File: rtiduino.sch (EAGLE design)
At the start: 111 parts, among them IC7 LM358D, J1 DCJ0202, J2 3.5MM-JACK, J3 2.5MM-JACK, Q2 16MHz, T1 NDT2955, T2 FDN340P, U1 ATMEGA2560AU, U10 AQV252G, U11 AQV252G, U12 AQV252G, U13 AQV252G, U14 AQV252G, U15 AQV252G, U16 AQV252G, U17 AQV252G, U2 LDU240S500, U20 AQV252G, U21 AQV252G, U22 AQV252G, U23 AQV252G, U24 AQV252G, U25 AQV252G, U26 AQV252G, U27 AQV252G, U3 LM2594HVM-3.3, U30 AQV252G, U31 AQV252G, U32 AQV252G, U33 AQV252G, U34 AQV252G, U35 AQV252G, U36 AQV252G, U37 AQV252G, U4 FT232RL, U5 FOD852

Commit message: Latest version with * fixed PSU arrangement * more caps * connectors moved outwards
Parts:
- removed C18: (no value), resistor:C-EUC0805K
- removed IC7: LM358D, linear:LM358D
- removed R10, R6: 10k, rcl:R-EU_R0805
- removed RESET-EN: (no value), jumper:SJ
- removed SV1: (no value), con-lstb:MA03-1
- removed T1: NDT2955, zetex:PMOSSOT223
- removed T2: FDN340P, zetex:PMOSSOT23
- removed U2: LDU240S500, RTI:LDU240S500
- added C19, C20, C21: (no value), resistor:C-EUC1210K
- added C22: (no value), rcl:C-EUC0805K
- added C23: 68uF, rcl:CPOL-EUE5-13
- added D3: SF37, farnell-parts:SF37
- added JP1: (no value), jumper:JP2E
- added L2: (no value), rcl:L-EU6000-XXX-RC
- added PAD1: VIN, wirepad:WIREPAD4,16O1,6
- added PAD2: GND, wirepad:WIREPAD4,16O1,6
- added PAD3: LED_VCC, wirepad:WIREPAD4,16O1,6
- added PAD4: LED_GND, wirepad:WIREPAD4,16O1,6
- added R2: 0R, resistor:R-EU_R0805
- C1, C10, C11, C14, C15, C16, C2, C3, C4, C9: device rcl:C-EU -> rcl:C-EUC0805K
- C12, C17: value 100n -> (none); device rcl:C-EU -> resistor:C-EUC1210K
- C13: value 100n -> (none); device rcl:C-EU -> rcl:C-EUC0805K
- C5: device resistor:CPOL-EUE3.5-10 -> rcl:CPOL-EUE5-13
- C8: device resistor:C-EUC0805K -> resistor:C-EUC1210K
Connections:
- removed net 5VREG: C18.1, C6.+, C7.+, C8.1, L1.2, R10.2, TP1.TP, U3.FB
- removed net CMP: C13.2, IC7A.+IN, R10.1, R6.2
- removed net DTR: C12.1, RESET-EN.1, RESET-EN.2, U4.DTR#
- removed net GATE_CMD: IC7B.-IN, IC7B.OUT, T1.G, T2.G
- removed net RXD3: R11.2, U1.PJ0(RXD3/PCINT9)
- removed net TXD3: R12.2, U1.PJ1(TXD3/PCINT10)
- new net RXD: JP1.1, R11.2, U1.(RXD1/INT2)PD2, U1.PJ0(RXD3/PCINT9)
- new net TXD: JP1.2, R12.2, U1.(TXD1/INT3)PD3, U1.PJ1(TXD3/PCINT10)
- net +3V3: no longer IC7A.-IN
- net +5V: now also C12.1, C6.+, C7.+, C8.1, L1.2, R2.1, R2.2, TP1.TP, U3.FB; no longer C16.1, C17.2, IC7P.V+, R7.2, R9.2, T1.S, T2.S, U4.RESET#, U4.VCC5I, U4.VCCIO
- net GND: now also C12.2, C13.2, C17.2, C19.2, C20.2, C21.2, C22.2, C23.-, JP1.3, PAD2.P; no longer C13.1, C17.1, C18.2, IC7P.V-, R6.1, SV1.1, U2.-VIN, U2.-VIN_2
- net LED_GND: now also PAD4.P; no longer U2.-VOUT, U2.-VOUT_2
- net LED_VCC: now also PAD3.P; no longer U2.+VOUT, U2.+VOUT_2
- net N$4: now also C20.1, C21.1, C22.1, C23.+, D3.C, L2.1; no longer IC7A.OUT, IC7B.+IN
- net N$43: now also C13.1, C17.1, C19.1, L2.2, U3.VIN; no longer S1.P, S1.P1
- net RESET: now also S1.P, S1.P1; no longer C12.2
- net RXD2: no longer SV1.3
- net TXD2: no longer SV1.2
- net USBVCC: now also C16.1, R7.2, R9.2, U4.RESET#, U4.VCC5I, U4.VCCIO; no longer T1.D, T2.D
- net VIN: now also D3.A, PAD1.P; no longer U2.+VIN, U2.+VIN_2, U3.VIN
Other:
- moved on the sheet: C5

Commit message: Update wih Superdome PCB
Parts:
- removed C13, C22: (no value), rcl:C-EUC0805K
- removed C17, C19, C20, C21: (no value), resistor:C-EUC1210K
- removed C23: 68uF, rcl:CPOL-EUE5-13
- removed D1: 1N5817-B, diode:1N5817-B
- removed D3: SF37, farnell-parts:SF37
- removed PAD1: VIN, wirepad:WIREPAD4,16O1,6
- removed PAD2: GND, wirepad:WIREPAD4,16O1,6
- removed PAD3: LED_VCC, wirepad:WIREPAD4,16O1,6
- removed PAD4: LED_GND, wirepad:WIREPAD4,16O1,6
- removed R2: 0R, resistor:R-EU_R0805
- added C18, C24, C25, C26, C27, C28, C30, C31: 100nF, rcl:C-EUC0805K
- added C29, C32: 4.7uF, rcl:C-EUC0805K
- added C42, C43, C44, C45, C46: 100n, rcl:C-EUC0805K
- added D4: BAT54C, diode:BAT54C
- added D5: MBRS130, diode:DIODE-DO214AA
- added F2: 500mA, rcl:L-EUL1812
- added J4: USB PROG, CC11x:47346-0001
- added JP2: (no value), pinhead:PINHD-1X6
- added JP3: (no value), pinhead:PINHD-2X8
- added L3: 330uH (DO3308P-334), inductor-coilcraft:DO3316P
- added R10: 10K, resistor:R-EU_R0805
- added R3, R6: 1k, rcl:R-EU_R0805
- added R40, R41: 1K, resistor:R-EU_R0805
- added R42, R43, R44, R45, R46: 10k, resistor:R-EU_R0805
- added R8: 4K7, resistor:R-EU_R0805
- added RESET-EN: (no value), jumper:SJ
- added RX1, TX1: (no value), led:LED0805ROUND
- added U2: FT232RL, SmartPrj:FT232RL
- added U6: LED-DRIVER, RTI:LED-DRIVER
- C12: value (none) -> 10UF; device resistor:C-EUC1210K -> RTI:EEE-FK1J100P-CASE-D
- C6: device resistor:CPOL-EUR/2012-12R -> rcl:CPOL-EUE5-13
- C7: value 68uF -> 100uF; device resistor:CPOL-EUR/2012-12R -> rcl:CPOL-EUE5-13
- C8: value (none) -> 47UF; device resistor:C-EUC1210K -> RTI:EEE-FK1J470P-CASE-F
- J3: value 2.5MM-JACK -> 2.5MM-JACKPRO; device RTI:2.5MM-JACK -> RTI:2.5MM-JACKPRO
- L1: value 100uH -> 3uH; device inductors:SBC10 -> RTI:WE-TPC-744053003_5818/5828
- L2: value (none) -> DR73-680-R; device rcl:L-EU6000-XXX-RC -> RTI:DR73-680-R
- U3: value LM2594HVM-3.3 -> LM2594HVM-5.0
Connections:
- new net +3V3PROG: C24.2, U2.VCC30
- new net N$50: RX1.C, U2.GPIO1
- new net N$52: TX1.C, U2.GPIO0
- new net N$58: R3.1, RX1.A
- new net N$62: R6.1, TX1.A
- new net N$63: F2.2, J4.1
- new net N$66: C26.1, RESET-EN.1, RESET-EN.2, U2.DTR#
- new net N$68: C16.2, R10.1, R8.2, U4.RESET#
- new net PROG_D+: J4.3, U2.USBDP
- new net PROG_D-: J4.2, U2.USBDM
- new net RXD1: U1.(RXD1/INT2)PD2
- new net RXDP: JP2.4, R40.1, U2.TXD
- new net RXD_PROG: R40.2, U1.(RXD0/PCIN8)PE0
- new net SCL: JP3.1, U1.(SCL/INT0)PD0
- new net SDA: JP3.3, U1.(SDA/INT1)PD1
- new net SW1: C46.1, JP3.7, R46.2, U1.PK0(ADC8/PCINT16)
- new net SW2: C45.1, JP3.9, R45.2, U1.PK1(ADC9/PCINT17)
- new net SW3: C44.1, JP3.11, R44.2, U1.PK2(ADC10/PCINT18)
- new net SW4: C43.1, JP3.13, R43.2, U1.PK3(ADC11/PCINT19)
- new net SW5: C42.1, JP3.15, R42.2, U1.PK4(ADC12/PCINT20)
- new net TXD1: U1.(TXD1/INT3)PD3
- new net TXDP: JP2.5, R41.1, U2.RXD
- new net TXD_PROG: R41.2, U1.(TXD0)PE1
- new net USBPROGVCC: C18.1, C25.1, C30.1, C31.1, C32.1, D4.A2, F2.1, JP2.3, R3.2, R6.2, U2.RESET#, U2.VCC5I, U2.VCCIO
- net +5V: now also C27.1, C28.1, C29.1, D4.CC, JP3.2, R42.1, R43.1, R44.1, R45.1, R46.1, U4.VCC5I, U4.VCCIO; no longer C12.1, C6.+, C8.1, R2.1, R2.2, U3.FB
- net GND: now also C16.1, C18.2, C24.1, C25.2, C27.2, C28.2, C29.2, C30.2, C31.2, C32.2, C42.2, C43.2, C44.2, C45.2, C46.2, D5.A, J4.5, JP2.1, JP3.10, JP3.12, JP3.14, JP3.16, JP3.4, JP3.8, R10.2, U2.AGND, U2.GND1, U2.GND2, U2.GND3, U2.TEST, U6.GIN; no longer C13.2, C16.2, C17.2, C19.2, C20.2, C21.2, C22.2, C23.-, D1.A, PAD2.P
- net LED_GND: now also U6.GOUT; no longer PAD4.P
- net LED_VCC: now also U6.VOUT; no longer PAD3.P
- net N$4: now also C6.+, L1.1, L3.2, U3.FB; no longer C20.1, C21.1, C22.1, C23.+, D3.C, L2.1
- net N$43: now also C8.1, L2.1, U6.VIN; no longer C13.1, C17.1, C19.1, L2.2, U3.VIN
- net N$48: now also D5.C, L3.1; no longer D1.C, L1.1
- net RESET: now also C26.2
- net RXD: no longer U1.(RXD1/INT2)PD2
- net RXD2: now also JP3.6
- net TXD: no longer U1.(TXD1/INT3)PD3
- net TXD2: now also JP3.5
- net USBVCC: now also D4.A1, R8.1; no longer C16.1, U4.RESET#, U4.VCC5I, U4.VCCIO
- net VIN: now also C12.1, L2.2, U3.VIN; no longer D3.A, PAD1.P
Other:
- note added: "** This is a 5V reg !! ** Keep leads as short as possible. Use isolated ground plane."
- note added: "30V Input"
- note added: "5V uC Switchmode Powersupply"
- note added: "Camera Shutter"
- note added: "Control Interface"
- note added: "Display Serial"
- note added: "Fire Button"
- note added: "Header for FTDI TTL-232R-5V cable. Needs manual reset as DTR is not connected."
- note added: "ICSP"
- note added: "LED Constant Current Driver"
- note added: "Onecall: 1267387"
- note added: "Onecall: 2082565"
- note added: "Onecall: 2457508"
- note added: "Onecall: 8812667"
- note added: "Onecall: 8812675"
- note added: "Pinout for FEMALE D-Sub connectors on PCB"
- note added: "Place close to U2"
- note added: "Place close to U4"
- note added: "Programming/Debug Interfaces"
- note added: "RS: 715-3031"
- note added: "Screen Interface"
- note added: "Status LEDs"
- note added: "UI Switches"
- note added: "USB Arduino Programmer"
- note added: "USB Voltage Combiner"
- note removed: "LED PSU"
- note removed: "This is the pin out if FEMALE D-subs are used on the PCB"
- note removed: "This is the pin out if FEMALE d-subs are used on the board"

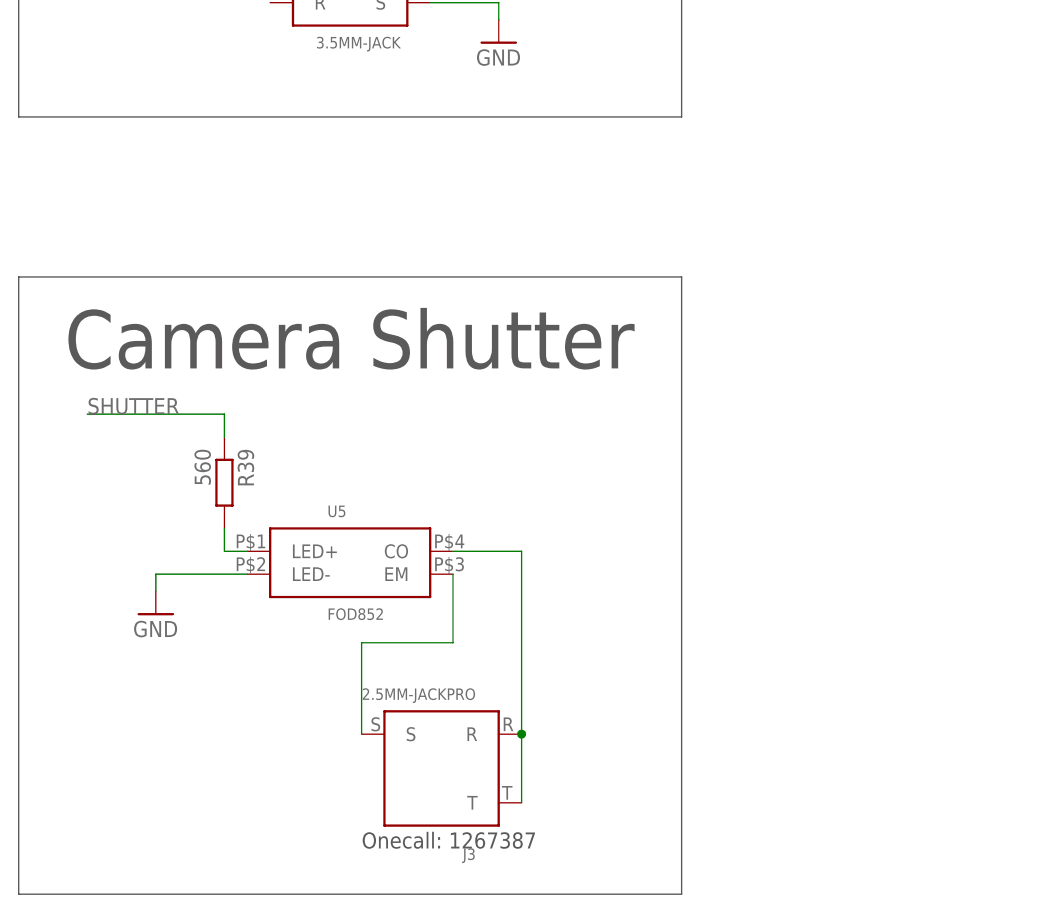
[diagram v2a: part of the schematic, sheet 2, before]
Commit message: Tweak to camera shutter trigger (split focus and shutter), tweak to serial programming, misc fixes
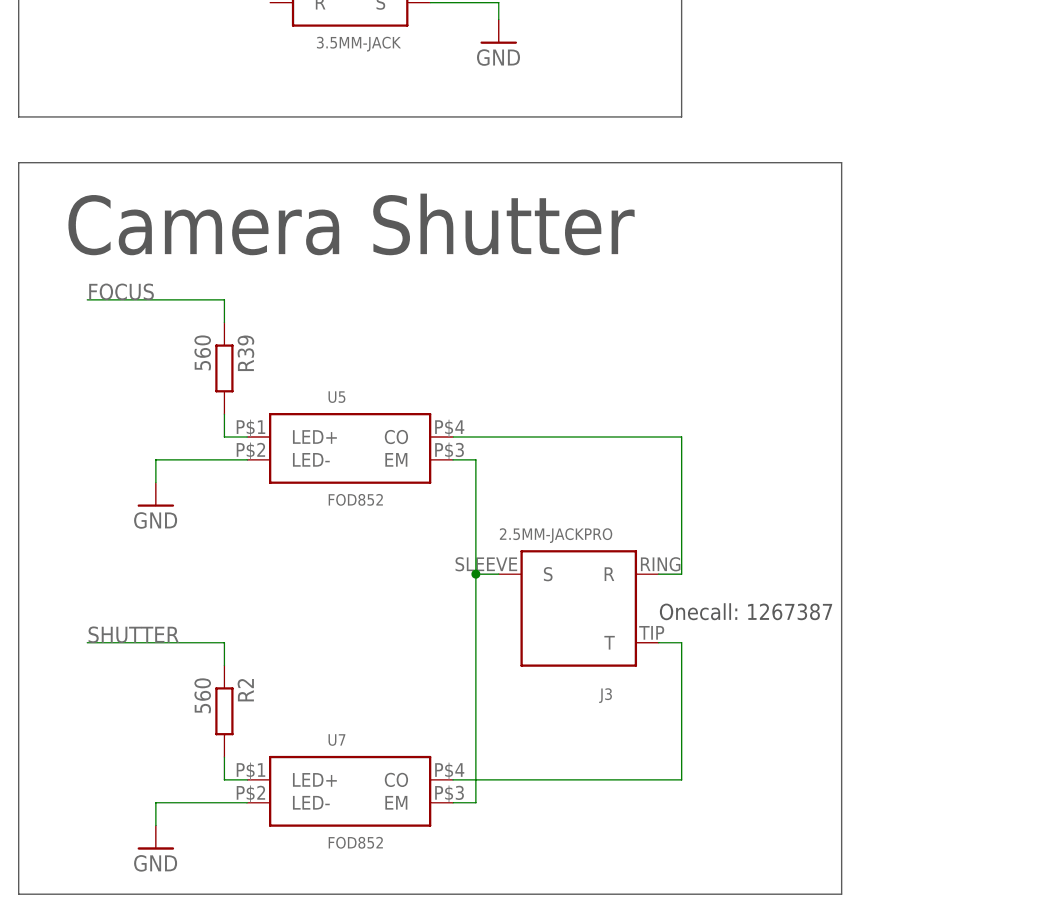
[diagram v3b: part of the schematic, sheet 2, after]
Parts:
- added C13: 100nF, rcl:C-EUC0805K
- added R2: 560, resistor:R-EU_R0805
- added RESET-EN1: (no value), jumper:SJ
- added U7: FOD852, RTI:FOD852
- L, RX, RX1, TX, TX1: device led:LED0805ROUND -> led:LEDCHIP-LED0805
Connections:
- net N$66 renamed DTR
- removed net N$51: J3.R, J3.T, U5.CO
- new net CAM_GND: J3.S, U5.EM, U7.EM
- new net CAM_RING: J3.R, U5.CO
- new net CAM_SHUTTER: J3.T, U7.CO
- new net DTRP: C13.1, JP2.2, RESET-EN1.1, RESET-EN1.2
- new net FOCUS: R39.1, U1.(TOSC2)PG3
- net GND: now also U7.LED-
- net N$61: now also R2.2, U7.LED+; no longer J3.S, U5.EM
- net RESET: now also C13.2
- net SHUTTER: now also R2.1; no longer R39.1
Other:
- moved on the sheet: J3, R39, U5

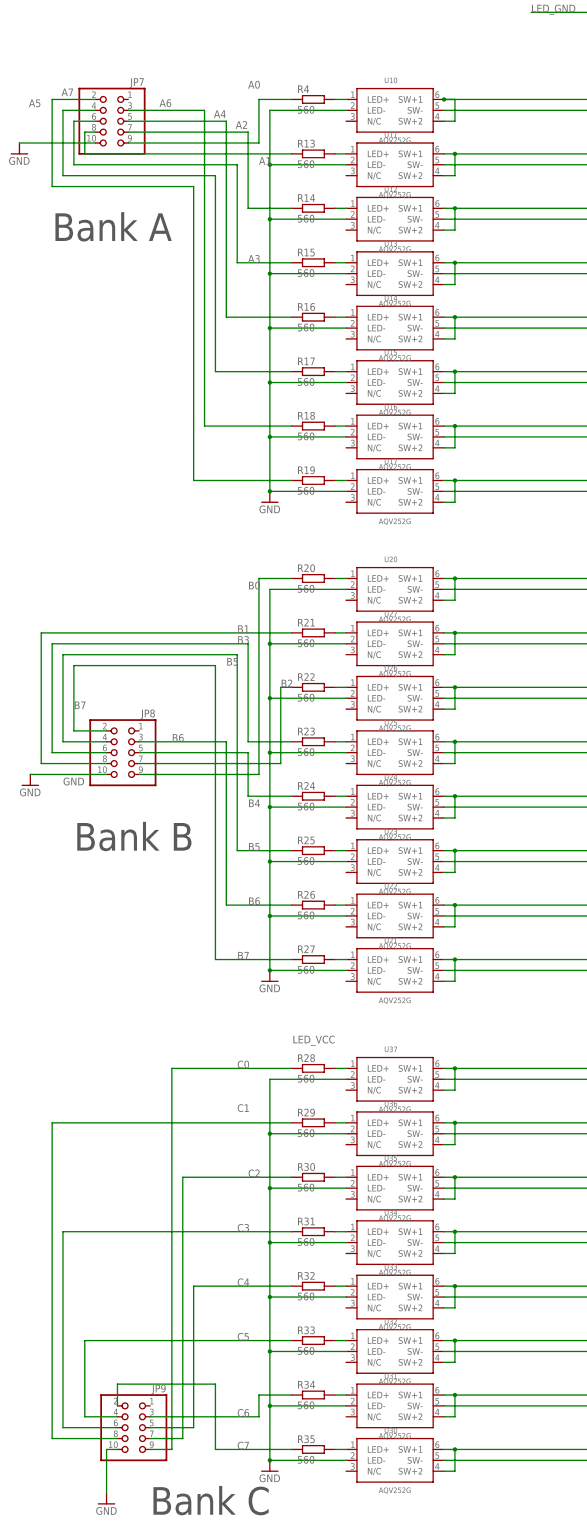
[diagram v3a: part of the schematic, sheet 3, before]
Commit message: Version 1.3 of RTIDuino and updated order sheet
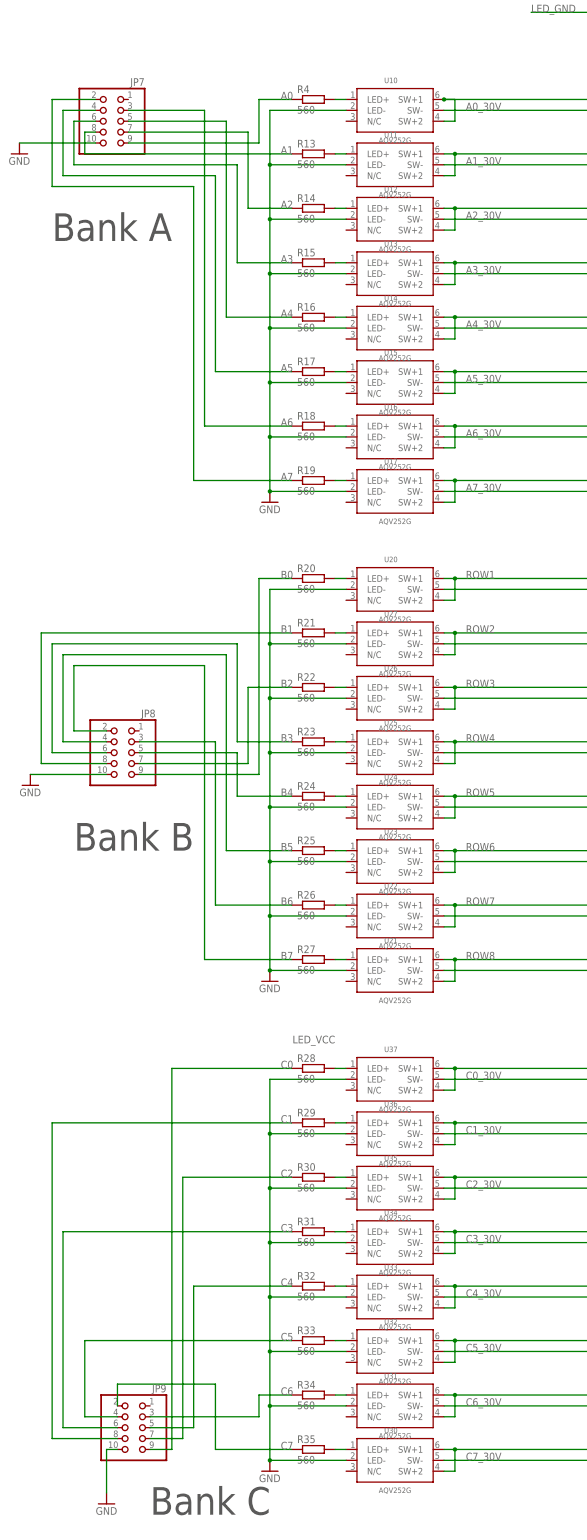
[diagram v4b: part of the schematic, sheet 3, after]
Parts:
- added JP4: (no value), pinhead:PINHD-1X2
- C1, C10, C14, C15, C16, C4, C42, C43, C44, C45, C46, C9: value 100n -> 100nF
- C11, C2, C3: value 22p -> 22pF
- C12: value 10UF -> 10uF
- C8: value 47UF -> 47uF
- R3, R6, R7, R9: value 1k -> 1K
- R42, R43, R44, R45, R46: value 10k -> 10K
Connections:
- net N$11 renamed A4_30V
- net N$14 renamed C6_30V
- net N$33 renamed A0_30V
- net N$34 renamed C0_30V
- net N$35 renamed A1_30V
- net N$36 renamed A2_30V
- net N$37 renamed A3_30V
- net N$38 renamed C2_30V
- net N$39 renamed C3_30V
- net N$40 renamed C4_30V
- net N$41 renamed C5_30V
- net N$42 renamed C7_30V
- net N$45 renamed A5_30V
- net N$46 renamed A6_30V
- net N$47 renamed A7_30V
- net N$49 renamed C1_30V
- net FOCUS: now also JP4.1
- net SHUTTER: now also JP4.2

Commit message: UPDATES
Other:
- note added: "Quarter A"
- note added: "Quarter B"
- note added: "Quarter C"
- note added: "Quarter D"
